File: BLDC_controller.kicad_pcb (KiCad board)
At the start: 4 copper layers, 50 x 35 mm, 95 parts, among them P2 CONN_01X06, P3 CONN_01X05, P5 CONN_01X05, Q1 PSMN2R0-30YLD, Q2 PSMN2R0-30YLD, Q3 PSMN2R0-30YLD, Q4 PSMN2R0-30YLD, Q5 PSMN2R0-30YLD, Q6 PSMN2R0-30YLD

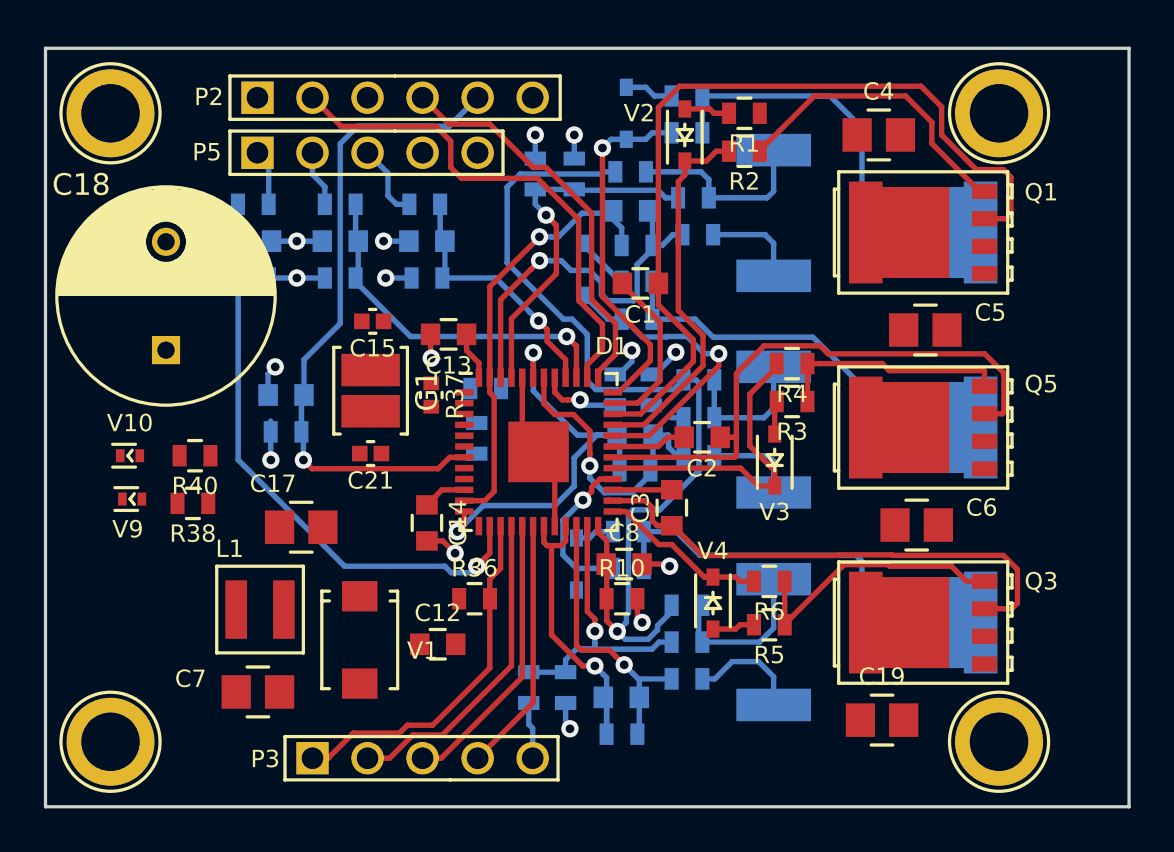
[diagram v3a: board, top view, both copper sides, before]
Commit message: keepouts added under sense resistors
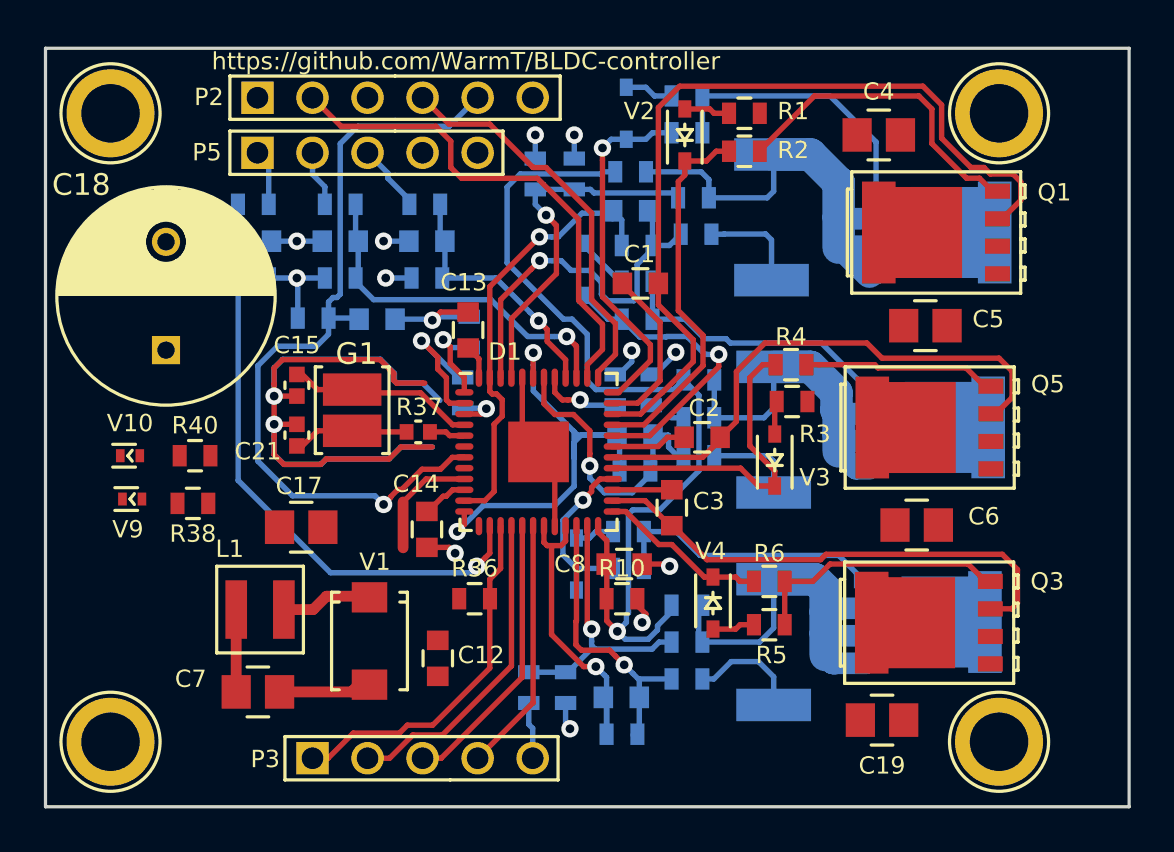
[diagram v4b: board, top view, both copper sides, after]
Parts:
- C15, C21: value C -> 10p
- moved C16 5.47 mm to (150.3, 91.5), turned to 0 degrees
- moved R39 5.40 mm to (147.3, 91.5)
- moved C15 4.58 mm to (146.6, 94.5), turned to 270 degrees
- moved C21 3.50 mm to (146.6, 96.8), turned to 90 degrees
- moved R29 2.71 mm to (154.6, 92.1), turned to 90 degrees
- moved R47 2.20 mm to (154.2, 94.9)
- moved R37 1.80 mm to (152.2, 96.7), turned to 180 degrees
- moved G1 1.24 mm to (149.2, 95.7)
- moved C13 0.92 mm to (154.5, 92.0), turned to 90 degrees
- moved C12 0.65 mm to (153.1, 107.2), turned to 270 degrees
- moved Q2 0.65 mm to (176.2, 87.5)
- moved Q1 0.60 mm to (176.1, 87.5)
- moved V1 0.45 mm to (149.9, 106.3)
- moved Q6 0.35 mm to (175.8, 96.5)
- moved Q5 0.30 mm to (175.8, 96.5)
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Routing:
- net GND: track 33.6 -> 81.5 mm, vias 8 -> 9
- net U_SENSE_P: track 8.90 -> 21.1 mm
- net W_SENSE_P: track 7.16 -> 19.3 mm
- net V_SENSE_P: track 6.58 -> 17.6 mm
- net /SW: track 0.00 -> 8.90 mm
- net /OSC_IN: track 0.00 -> 7.60 mm
- net /OP4N: track 0.00 -> 7.04 mm, vias 0 -> 1
- net /NRST: track 30.4 -> 37.3 mm
- net Net-(C21-Pad1): track 0.00 -> 6.60 mm
- net +3V3: track 13.2 -> 18.5 mm
- net /OP4P: track 0.00 -> 4.18 mm, vias 0 -> 1
- net Net-(D1-Pad3): track 0.00 -> 2.22 mm, vias 0 -> 1
- net /HSV: track 10.8 -> 8.63 mm
- net (no net): track 1.80 -> 0.00 mm, vias 1 -> 0
- net /V_ADC: track 20.7 -> 22.4 mm
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- added copper zone on B.Cu, net GND
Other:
- rule trace_min: 0.2 -> 0.15
- board text added: "https://github.com/WarmT/BLDC-controller"

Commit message: Layout ready for 1st review
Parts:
- removed C18: 680u, project_footprints:C_Radial_D10_L25_P5
- added REF**: VIA-0.8mm-0.4mm, project_footprints:VIA-0.8mm-0.4mm, F.Cu at (151.2, 97.8)
- added REF**: VIA-0.8mm-0.4mm, project_footprints:VIA-0.8mm-0.4mm, F.Cu at (149.9, 93.2)
- added REF**: VIA-1.2mm-0.8mm, project_footprints:VIA-1.2mm-0.8mm, F.Cu at (166.2, 113.2)
- added REF**: VIA-0.8mm-0.4mm, project_footprints:VIA-0.8mm-0.4mm, F.Cu at (147.8, 93.2)
- added REF**: VIA-0.8mm-0.4mm, project_footprints:VIA-0.8mm-0.4mm, F.Cu at (148.9, 93.2)
- added REF**: VIA-1.2mm-0.8mm, project_footprints:VIA-1.2mm-0.8mm, F.Cu at (172.8, 102.3)
- added REF**: VIA-1.2mm-0.8mm, project_footprints:VIA-1.2mm-0.8mm, F.Cu at (180.1, 100.7)
- added REF**: VIA-1.2mm-0.8mm, project_footprints:VIA-1.2mm-0.8mm, F.Cu at (174.9, 112.0)
- added REF**: VIA-1.2mm-0.8mm, project_footprints:VIA-1.2mm-0.8mm, F.Cu at (174.9, 109.9)
- added REF**: VIA-1.2mm-0.8mm, project_footprints:VIA-1.2mm-0.8mm, F.Cu at (174.4, 100.4)
- added REF**: VIA-1.2mm-0.8mm, project_footprints:VIA-1.2mm-0.8mm, F.Cu at (173.8, 91.3)
- added REF**: VIA-1.2mm-0.8mm, project_footprints:VIA-1.2mm-0.8mm, F.Cu at (179.5, 91.0)
- added REF**: VIA-1.2mm-0.8mm, project_footprints:VIA-1.2mm-0.8mm, F.Cu at (176.8, 84.0)
- added REF**: VIA-0.8mm-0.4mm, project_footprints:VIA-0.8mm-0.4mm, F.Cu at (149.8, 98.1)
- added REF**: VIA-1.2mm-0.8mm, project_footprints:VIA-1.2mm-0.8mm, F.Cu at (177.0, 79.0)
- added REF**: VIA-1.2mm-0.8mm, project_footprints:VIA-1.2mm-0.8mm, F.Cu at (177.0, 80.2)
- added REF**: VIA-1.2mm-0.8mm, project_footprints:VIA-1.2mm-0.8mm, F.Cu at (175.0, 80.2)
- added REF**: VIA-1.2mm-0.8mm, project_footprints:VIA-1.2mm-0.8mm, F.Cu at (175.0, 79.0)
- added REF**: VIA-1.2mm-0.8mm, project_footprints:VIA-1.2mm-0.8mm, F.Cu at (170.9, 81.8)
- added REF**: VIA-1.2mm-0.8mm, project_footprints:VIA-1.2mm-0.8mm, F.Cu at (169.7, 81.8)
- added REF**: VIA-1.2mm-0.8mm, project_footprints:VIA-1.2mm-0.8mm, F.Cu at (168.5, 81.8)
- added REF**: VIA-1.2mm-0.8mm, project_footprints:VIA-1.2mm-0.8mm, F.Cu at (167.3, 81.8)
- added REF**: VIA-1.2mm-0.8mm, project_footprints:VIA-1.2mm-0.8mm, F.Cu at (170.9, 80.7)
- added REF**: VIA-1.2mm-0.8mm, project_footprints:VIA-1.2mm-0.8mm, F.Cu at (169.7, 80.7)
- added REF**: VIA-0.8mm-0.4mm, project_footprints:VIA-0.8mm-0.4mm, F.Cu at (148.7, 98.1)
- added REF**: VIA-1.2mm-0.8mm, project_footprints:VIA-1.2mm-0.8mm, F.Cu at (168.5, 80.7)
- added REF**: VIA-1.2mm-0.8mm, project_footprints:VIA-1.2mm-0.8mm, F.Cu at (167.3, 80.7)
- added REF**: VIA-1.2mm-0.8mm, project_footprints:VIA-1.2mm-0.8mm, F.Cu at (170.9, 79.5)
- added REF**: VIA-1.2mm-0.8mm, project_footprints:VIA-1.2mm-0.8mm, F.Cu at (169.7, 79.5)
- added REF**: VIA-1.2mm-0.8mm, project_footprints:VIA-1.2mm-0.8mm, F.Cu at (168.5, 79.5)
- added REF**: VIA-1.2mm-0.8mm, project_footprints:VIA-1.2mm-0.8mm, F.Cu at (169.7, 103.6)
- added REF**: VIA-1.2mm-0.8mm, project_footprints:VIA-1.2mm-0.8mm, F.Cu at (168.5, 103.6)
- added REF**: VIA-1.2mm-0.8mm, project_footprints:VIA-1.2mm-0.8mm, F.Cu at (167.3, 103.6)
- added REF**: VIA-1.2mm-0.8mm, project_footprints:VIA-1.2mm-0.8mm, F.Cu at (170.9, 103.6)
- added REF**: VIA-1.2mm-0.8mm, project_footprints:VIA-1.2mm-0.8mm, F.Cu at (169.7, 102.4)
- added REF**: VIA-0.8mm-0.4mm, project_footprints:VIA-0.8mm-0.4mm, F.Cu at (146.6, 93.1)
- added REF**: VIA-1.2mm-0.8mm, project_footprints:VIA-1.2mm-0.8mm, F.Cu at (168.5, 102.4)
- added REF**: VIA-1.2mm-0.8mm, project_footprints:VIA-1.2mm-0.8mm, F.Cu at (167.3, 102.4)
- added REF**: VIA-1.2mm-0.8mm, project_footprints:VIA-1.2mm-0.8mm, F.Cu at (170.9, 102.4)
- added REF**: VIA-1.2mm-0.8mm, project_footprints:VIA-1.2mm-0.8mm, F.Cu at (169.7, 101.2)
- added REF**: VIA-1.2mm-0.8mm, project_footprints:VIA-1.2mm-0.8mm, F.Cu at (168.5, 101.2)
- added REF**: VIA-1.2mm-0.8mm, project_footprints:VIA-1.2mm-0.8mm, F.Cu at (167.3, 101.2)
- added REF**: VIA-1.2mm-0.8mm, project_footprints:VIA-1.2mm-0.8mm, F.Cu at (170.9, 101.2)
- added REF**: VIA-1.2mm-0.8mm, project_footprints:VIA-1.2mm-0.8mm, F.Cu at (184.2, 108.4)
- added REF**: VIA-1.2mm-0.8mm, project_footprints:VIA-1.2mm-0.8mm, F.Cu at (182.9, 108.4)
- added REF**: VIA-1.2mm-0.8mm, project_footprints:VIA-1.2mm-0.8mm, F.Cu at (181.8, 108.4)
- added REF**: VIA-0.8mm-0.4mm, project_footprints:VIA-0.8mm-0.4mm, F.Cu at (147.5, 98.2)
- added REF**: VIA-1.2mm-0.8mm, project_footprints:VIA-1.2mm-0.8mm, F.Cu at (184.2, 107.2)
- added REF**: VIA-1.2mm-0.8mm, project_footprints:VIA-1.2mm-0.8mm, F.Cu at (182.9, 107.2)
- added REF**: VIA-1.2mm-0.8mm, project_footprints:VIA-1.2mm-0.8mm, F.Cu at (181.8, 107.2)
- added REF**: VIA-1.2mm-0.8mm, project_footprints:VIA-1.2mm-0.8mm, F.Cu at (184.2, 106.0)
- added REF**: VIA-1.2mm-0.8mm, project_footprints:VIA-1.2mm-0.8mm, F.Cu at (182.9, 106.0)
- added REF**: VIA-1.2mm-0.8mm, project_footprints:VIA-1.2mm-0.8mm, F.Cu at (181.8, 106.0)
- added REF**: VIA-1.2mm-0.8mm, project_footprints:VIA-1.2mm-0.8mm, F.Cu at (184.2, 104.8)
- added REF**: VIA-1.2mm-0.8mm, project_footprints:VIA-1.2mm-0.8mm, F.Cu at (182.9, 104.8)
- added REF**: VIA-1.2mm-0.8mm, project_footprints:VIA-1.2mm-0.8mm, F.Cu at (181.8, 104.8)
- added REF**: VIA-1.2mm-0.8mm, project_footprints:VIA-1.2mm-0.8mm, F.Cu at (184.2, 99.6)
- added REF**: VIA-0.8mm-0.4mm, project_footprints:VIA-0.8mm-0.4mm, F.Cu at (145.5, 97.4)
- added REF**: VIA-1.2mm-0.8mm, project_footprints:VIA-1.2mm-0.8mm, F.Cu at (182.9, 99.6)
- added REF**: VIA-1.2mm-0.8mm, project_footprints:VIA-1.2mm-0.8mm, F.Cu at (181.8, 99.6)
- added REF**: VIA-1.2mm-0.8mm, project_footprints:VIA-1.2mm-0.8mm, F.Cu at (184.2, 98.4)
- added REF**: VIA-1.2mm-0.8mm, project_footprints:VIA-1.2mm-0.8mm, F.Cu at (182.9, 98.4)
- added REF**: VIA-1.2mm-0.8mm, project_footprints:VIA-1.2mm-0.8mm, F.Cu at (181.8, 98.4)
- added REF**: VIA-1.2mm-0.8mm, project_footprints:VIA-1.2mm-0.8mm, F.Cu at (184.2, 97.2)
- added REF**: VIA-1.2mm-0.8mm, project_footprints:VIA-1.2mm-0.8mm, F.Cu at (182.9, 97.2)
- added REF**: VIA-1.2mm-0.8mm, project_footprints:VIA-1.2mm-0.8mm, F.Cu at (181.8, 97.2)
- added REF**: VIA-1.2mm-0.8mm, project_footprints:VIA-1.2mm-0.8mm, F.Cu at (184.2, 96.0)
- added REF**: VIA-1.2mm-0.8mm, project_footprints:VIA-1.2mm-0.8mm, F.Cu at (182.9, 96.0)
- added REF**: VIA-0.8mm-0.4mm, project_footprints:VIA-0.8mm-0.4mm, F.Cu at (145.6, 93.9)
- added REF**: VIA-1.2mm-0.8mm, project_footprints:VIA-1.2mm-0.8mm, F.Cu at (181.8, 96.0)
- added REF**: VIA-1.2mm-0.8mm, project_footprints:VIA-1.2mm-0.8mm, F.Cu at (184.2, 90.7)
- added REF**: VIA-1.2mm-0.8mm, project_footprints:VIA-1.2mm-0.8mm, F.Cu at (182.9, 90.7)
- added REF**: VIA-1.2mm-0.8mm, project_footprints:VIA-1.2mm-0.8mm, F.Cu at (181.8, 90.7)
- added REF**: VIA-1.2mm-0.8mm, project_footprints:VIA-1.2mm-0.8mm, F.Cu at (184.2, 89.5)
- added REF**: VIA-1.2mm-0.8mm, project_footprints:VIA-1.2mm-0.8mm, F.Cu at (182.9, 89.5)
- added REF**: VIA-1.2mm-0.8mm, project_footprints:VIA-1.2mm-0.8mm, F.Cu at (181.8, 89.5)
- added REF**: VIA-1.2mm-0.8mm, project_footprints:VIA-1.2mm-0.8mm, F.Cu at (184.2, 88.3)
- added REF**: VIA-1.2mm-0.8mm, project_footprints:VIA-1.2mm-0.8mm, F.Cu at (182.9, 88.3)
- added REF**: VIA-1.2mm-0.8mm, project_footprints:VIA-1.2mm-0.8mm, F.Cu at (181.8, 88.3)
- added REF**: VIA-0.8mm-0.4mm, project_footprints:VIA-0.8mm-0.4mm, F.Cu at (152.2, 94.1)
- added REF**: VIA-1.2mm-0.8mm, project_footprints:VIA-1.2mm-0.8mm, F.Cu at (184.2, 87.1)
- added REF**: VIA-1.2mm-0.8mm, project_footprints:VIA-1.2mm-0.8mm, F.Cu at (182.9, 87.1)
- added REF**: VIA-1.2mm-0.8mm, project_footprints:VIA-1.2mm-0.8mm, F.Cu at (181.8, 87.1)
- added REF**: VIA-1.2mm-0.8mm, project_footprints:VIA-1.2mm-0.8mm, F.Cu at (157.0, 95.5)
- added REF**: VIA-1.2mm-0.8mm, project_footprints:VIA-1.2mm-0.8mm, F.Cu at (172.2, 114.5)
- added REF**: VIA-1.2mm-0.8mm, project_footprints:VIA-1.2mm-0.8mm, F.Cu at (171.1, 114.5)
- added REF**: VIA-1.2mm-0.8mm, project_footprints:VIA-1.2mm-0.8mm, F.Cu at (169.8, 114.5)
- added REF**: VIA-1.2mm-0.8mm, project_footprints:VIA-1.2mm-0.8mm, F.Cu at (168.7, 114.5)
- added REF**: VIA-1.2mm-0.8mm, project_footprints:VIA-1.2mm-0.8mm, F.Cu at (167.4, 114.5)
- added REF**: VIA-0.8mm-0.4mm, project_footprints:VIA-0.8mm-0.4mm, F.Cu at (151.0, 93.4)
- added REF**: VIA-1.2mm-0.8mm, project_footprints:VIA-1.2mm-0.8mm, F.Cu at (166.2, 114.5)
- added REF**: VIA-1.2mm-0.8mm, project_footprints:VIA-1.2mm-0.8mm, F.Cu at (172.2, 113.2)
- added REF**: VIA-1.2mm-0.8mm, project_footprints:VIA-1.2mm-0.8mm, F.Cu at (171.1, 113.2)
- added REF**: VIA-1.2mm-0.8mm, project_footprints:VIA-1.2mm-0.8mm, F.Cu at (169.8, 113.2)
- added REF**: VIA-1.2mm-0.8mm, project_footprints:VIA-1.2mm-0.8mm, F.Cu at (168.7, 113.2)
- added REF**: VIA-1.2mm-0.8mm, project_footprints:VIA-1.2mm-0.8mm, F.Cu at (167.4, 113.2)
- added REF**: VIA-1.2mm-0.8mm, project_footprints:VIA-1.2mm-0.8mm, F.Cu at (167.3, 79.5)
- moved V10 26.3 mm to (161.0, 112.1)
- moved R40 25.9 mm to (163.6, 112.1)
- moved V9 22.3 mm to (159.3, 109.0)
- moved R38 22.0 mm to (161.8, 109.1)
- moved C12 8.53 mm to (148.6, 99.9), turned to 180 degrees
- moved C1 4.24 mm to (161.6, 85.7)
- moved C19 3.52 mm to (177.0, 110.9), turned to 270 degrees
- moved REF** 3.48 mm to (182.0, 112.8)
- moved REF** 3.09 mm to (182.0, 81.3)
- moved C4 2.78 mm to (176.0, 81.9)
- moved R2 2.77 mm to (164.5, 83.4)
- moved R1 2.77 mm to (164.5, 81.7)
- moved C17 2.69 mm to (149.3, 102.1), turned to 180 degrees
- moved R7 2.48 mm to (170.2, 108.3)
- moved V2 2.38 mm to (162.2, 82.4)
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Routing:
- net GND: track 81.5 -> 114.7 mm, vias 9 -> 20
- net +12V: track 0.00 -> 25.7 mm, vias 0 -> 3
- net /OUTW: track 23.5 -> 37.0 mm, vias 0 -> 1
- net +3V3: track 18.5 -> 30.0 mm, vias 6 -> 9
- net /OUTU: track 39.3 -> 49.9 mm, vias 0 -> 1
- net V_SENSE_P: track 17.6 -> 7.63 mm, vias 0 -> 2
- net /HSU: track 14.8 -> 24.0 mm, vias 0 -> 2
- net U_SENSE_P: track 21.1 -> 12.4 mm, vias 0 -> 2
- net /HSV: track 8.63 -> 17.2 mm, vias 0 -> 2
- net /OUTV: track 25.1 -> 33.3 mm, vias 0 -> 1
- net /LSV: track 13.1 -> 20.6 mm, vias 0 -> 2
- net W_SENSE_P: track 19.3 -> 12.2 mm, vias 0 -> 2
- net /LSU: track 12.9 -> 19.8 mm, vias 0 -> 2
- net /LSW: track 13.5 -> 20.0 mm, vias 0 -> 2
- net /HSW: track 12.2 -> 18.6 mm, vias 0 -> 2
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- added copper zone on F.Cu, net +12V
- added copper zone on In1.Cu, net +12V
- added copper zone on In2.Cu, net +12V
- added copper zone on In1.Cu, net +3V3
- added copper zone on B.Cu, net /OUTU
- added copper zone on F.Cu, net /OUTU
- added copper zone on In2.Cu, net /OUTU
- added copper zone on B.Cu, net /OUTV
- added copper zone on F.Cu, net /OUTV
- added copper zone on In2.Cu, net /OUTV
- added copper zone on B.Cu, net /OUTW
- added copper zone on F.Cu, net /OUTW
- added copper zone on In2.Cu, net /OUTW
- added copper zone on F.Cu, net GND
- added copper zone on In2.Cu, net GND
- added copper zone on B.Cu, net U_SENSE_P
- added copper zone on B.Cu, net V_SENSE_P
- added copper zone on B.Cu, net W_SENSE_P
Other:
- board size 50 x 35 mm -> 50 x 38 mm
- rule trace_min: 0.15 -> 0.25
- board text added: "1"
- board text added: "2"
- board text added: "3"
- board text added: "4"
- board text added: "github.com/WarmT/BLDC-controller 1.0"
- board text removed: "https://github.com/WarmT/BLDC-controller"

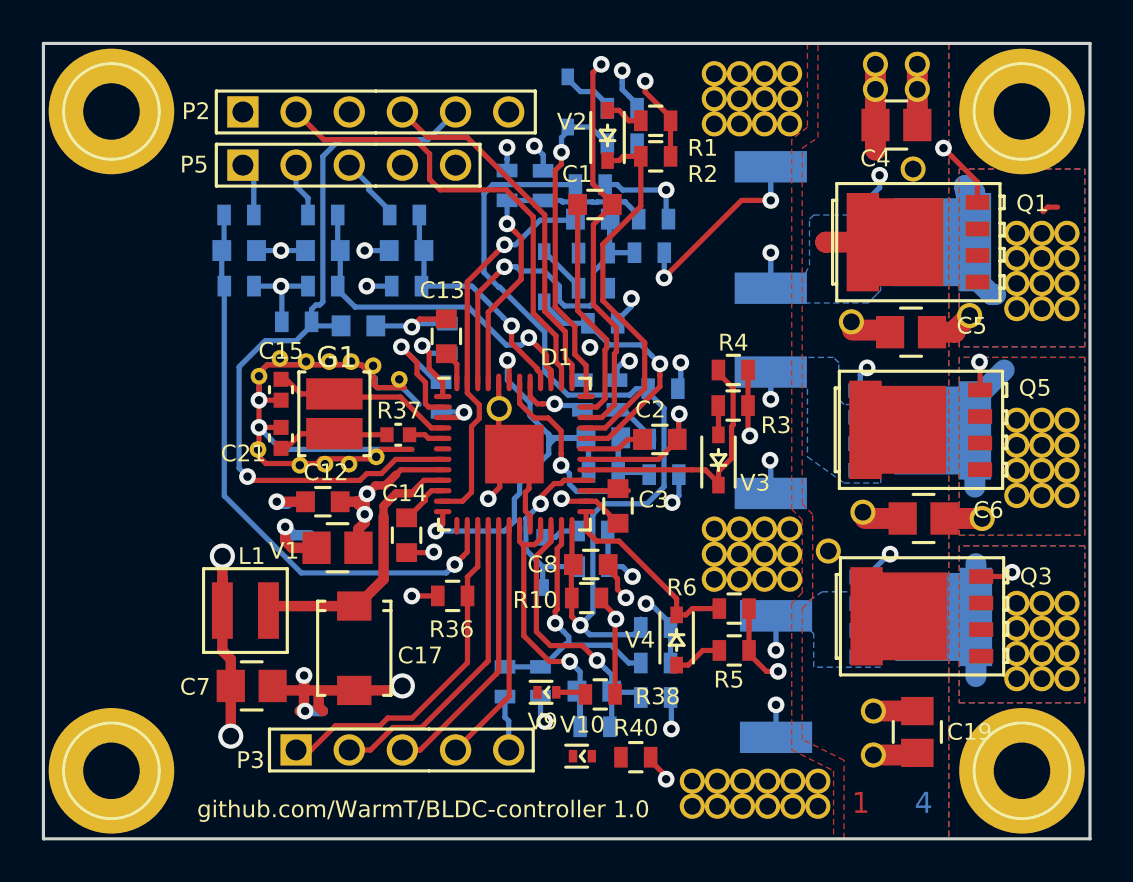
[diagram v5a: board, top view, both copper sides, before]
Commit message: change thermal vias smaller
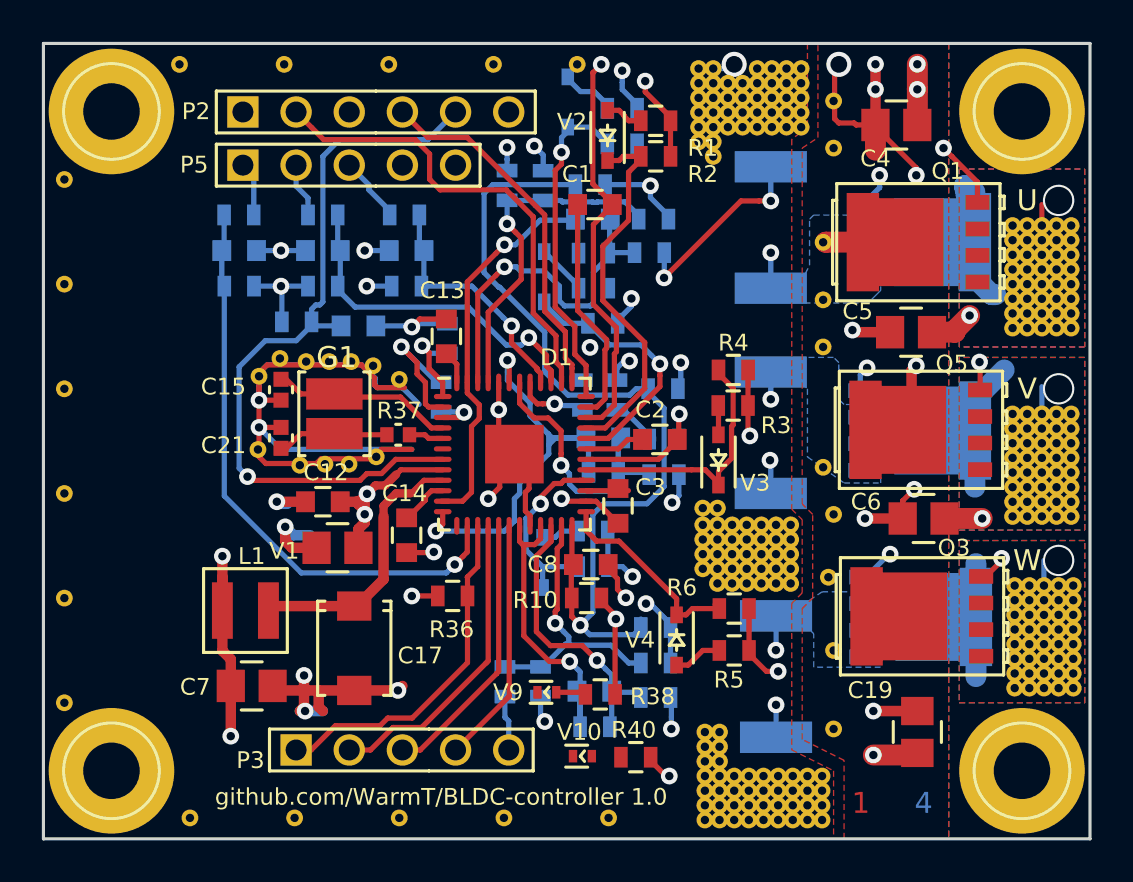
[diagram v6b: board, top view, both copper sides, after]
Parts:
- removed the REF** at (166.2, 113.2)
- removed the REF** at (172.8, 102.3)
- removed the REF** at (180.1, 100.7)
- removed the REF** at (174.9, 112.0)
- removed the REF** at (174.9, 109.9)
- removed the REF** at (174.4, 100.4)
- removed the REF** at (173.8, 91.3)
- removed the REF** at (179.5, 91.0)
- removed the REF** at (176.8, 84.0)
- removed the REF** at (177.0, 79.0)
- removed the REF** at (177.0, 80.2)
- removed the REF** at (175.0, 80.2)
- removed the REF** at (175.0, 79.0)
- removed the REF** at (170.9, 81.8)
- removed the REF** at (169.7, 81.8)
- removed the REF** at (168.5, 81.8)
- removed the REF** at (167.3, 81.8)
- removed the REF** at (170.9, 80.7)
- removed the REF** at (169.7, 80.7)
- removed the REF** at (168.5, 80.7)
- removed the REF** at (167.3, 80.7)
- removed the REF** at (170.9, 79.5)
- removed the REF** at (169.7, 79.5)
- removed the REF** at (168.5, 79.5)
- removed the REF** at (169.7, 103.6)
- removed the REF** at (168.5, 103.6)
- removed the REF** at (167.3, 103.6)
- removed the REF** at (170.9, 103.6)
- removed the REF** at (169.7, 102.4)
- removed the REF** at (168.5, 102.4)
- removed the REF** at (167.3, 102.4)
- removed the REF** at (170.9, 102.4)
- removed the REF** at (169.7, 101.2)
- removed the REF** at (168.5, 101.2)
- removed the REF** at (167.3, 101.2)
- removed the REF** at (170.9, 101.2)
- removed the REF** at (184.2, 108.4)
- removed the REF** at (182.9, 108.4)
- removed the REF** at (181.8, 108.4)
- removed the REF** at (184.2, 107.2)
- removed the REF** at (182.9, 107.2)
- removed the REF** at (181.8, 107.2)
- removed the REF** at (184.2, 106.0)
- removed the REF** at (182.9, 106.0)
- removed the REF** at (181.8, 106.0)
- removed the REF** at (184.2, 104.8)
- removed the REF** at (182.9, 104.8)
- removed the REF** at (181.8, 104.8)
- removed the REF** at (184.2, 99.6)
- removed the REF** at (182.9, 99.6)
- removed the REF** at (181.8, 99.6)
- removed the REF** at (184.2, 98.4)
- removed the REF** at (182.9, 98.4)
- removed the REF** at (181.8, 98.4)
- removed the REF** at (184.2, 97.2)
- removed the REF** at (182.9, 97.2)
- removed the REF** at (181.8, 97.2)
- removed the REF** at (184.2, 96.0)
- removed the REF** at (182.9, 96.0)
- removed the REF** at (181.8, 96.0)
- removed the REF** at (184.2, 90.7)
- removed the REF** at (182.9, 90.7)
- removed the REF** at (181.8, 90.7)
- removed the REF** at (184.2, 89.5)
- removed the REF** at (182.9, 89.5)
- removed the REF** at (181.8, 89.5)
- removed the REF** at (184.2, 88.3)
- removed the REF** at (182.9, 88.3)
- removed the REF** at (181.8, 88.3)
- removed the REF** at (184.2, 87.1)
- removed the REF** at (182.9, 87.1)
- removed the REF** at (181.8, 87.1)
- removed the REF** at (157.0, 95.5)
- removed the REF** at (172.2, 114.5)
- removed the REF** at (171.1, 114.5)
- removed the REF** at (169.8, 114.5)
- removed the REF** at (168.7, 114.5)
- removed the REF** at (167.4, 114.5)
- removed the REF** at (166.2, 114.5)
- removed the REF** at (172.2, 113.2)
- removed the REF** at (171.1, 113.2)
- removed the REF** at (169.8, 113.2)
- removed the REF** at (168.7, 113.2)
- removed the REF** at (167.4, 113.2)
- removed the REF** at (167.3, 79.5)
- added REF**: VIA-0.8mm-0.4mm, project_footprints:VIA-0.8mm-0.4mm, F.Cu at (162.2, 115.0)
- added REF**: VIA-0.8mm-0.4mm, project_footprints:VIA-0.8mm-0.4mm, F.Cu at (136.2, 94.5)
- added REF**: VIA-0.8mm-0.4mm, project_footprints:VIA-0.8mm-0.4mm, F.Cu at (181.6, 96.4)
- added REF**: VIA-0.8mm-0.4mm, project_footprints:VIA-0.8mm-0.4mm, F.Cu at (184.3, 95.7)
- added REF**: VIA-0.8mm-0.4mm, project_footprints:VIA-0.8mm-0.4mm, F.Cu at (183.7, 95.7)
- added REF**: VIA-0.8mm-0.4mm, project_footprints:VIA-0.8mm-0.4mm, F.Cu at (182.9, 95.7)
- added REF**: VIA-0.8mm-0.4mm, project_footprints:VIA-0.8mm-0.4mm, F.Cu at (182.2, 95.7)
- added REF**: VIA-0.8mm-0.4mm, project_footprints:VIA-0.8mm-0.4mm, F.Cu at (181.7, 103.9)
- added REF**: VIA-0.8mm-0.4mm, project_footprints:VIA-0.8mm-0.4mm, F.Cu at (184.3, 91.6)
- added REF**: VIA-0.8mm-0.4mm, project_footprints:VIA-0.8mm-0.4mm, F.Cu at (183.7, 91.6)
- added REF**: VIA-0.8mm-0.4mm, project_footprints:VIA-0.8mm-0.4mm, F.Cu at (182.9, 91.6)
- added REF**: VIA-0.8mm-0.4mm, project_footprints:VIA-0.8mm-0.4mm, F.Cu at (182.2, 91.6)
- added REF**: VIA-0.8mm-0.4mm, project_footprints:VIA-0.8mm-0.4mm, F.Cu at (136.2, 99.5)
- added REF**: VIA-0.8mm-0.4mm, project_footprints:VIA-0.8mm-0.4mm, F.Cu at (181.6, 91.6)
- added REF**: VIA-0.8mm-0.4mm, project_footprints:VIA-0.8mm-0.4mm, F.Cu at (184.3, 90.9)
- added REF**: VIA-0.8mm-0.4mm, project_footprints:VIA-0.8mm-0.4mm, F.Cu at (183.7, 90.9)
- added REF**: VIA-0.8mm-0.4mm, project_footprints:VIA-0.8mm-0.4mm, F.Cu at (182.9, 90.9)
- added REF**: VIA-0.8mm-0.4mm, project_footprints:VIA-0.8mm-0.4mm, F.Cu at (182.2, 90.9)
- added REF**: VIA-0.8mm-0.4mm, project_footprints:VIA-0.8mm-0.4mm, F.Cu at (181.6, 90.9)
- added REF**: VIA-0.8mm-0.4mm, project_footprints:VIA-0.8mm-0.4mm, F.Cu at (184.3, 90.2)
- added REF**: VIA-0.8mm-0.4mm, project_footprints:VIA-0.8mm-0.4mm, F.Cu at (183.7, 90.2)
- added REF**: VIA-0.8mm-0.4mm, project_footprints:VIA-0.8mm-0.4mm, F.Cu at (182.9, 90.2)
- added REF**: VIA-0.8mm-0.4mm, project_footprints:VIA-0.8mm-0.4mm, F.Cu at (182.2, 90.2)
- added REF**: VIA-0.8mm-0.4mm, project_footprints:VIA-0.8mm-0.4mm, F.Cu at (136.2, 104.5)
- added REF**: VIA-0.8mm-0.4mm, project_footprints:VIA-0.8mm-0.4mm, F.Cu at (181.6, 90.2)
- added REF**: VIA-0.8mm-0.4mm, project_footprints:VIA-0.8mm-0.4mm, F.Cu at (184.3, 89.5)
- added REF**: VIA-0.8mm-0.4mm, project_footprints:VIA-0.8mm-0.4mm, F.Cu at (183.7, 89.5)
- added REF**: VIA-0.8mm-0.4mm, project_footprints:VIA-0.8mm-0.4mm, F.Cu at (182.9, 89.5)
- added REF**: VIA-0.8mm-0.4mm, project_footprints:VIA-0.8mm-0.4mm, F.Cu at (182.2, 89.5)
- added REF**: VIA-0.8mm-0.4mm, project_footprints:VIA-0.8mm-0.4mm, F.Cu at (181.6, 89.5)
- added REF**: VIA-0.8mm-0.4mm, project_footprints:VIA-0.8mm-0.4mm, F.Cu at (184.3, 88.8)
- added REF**: VIA-0.8mm-0.4mm, project_footprints:VIA-0.8mm-0.4mm, F.Cu at (183.7, 88.8)
- added REF**: VIA-0.8mm-0.4mm, project_footprints:VIA-0.8mm-0.4mm, F.Cu at (182.9, 88.8)
- added REF**: VIA-0.8mm-0.4mm, project_footprints:VIA-0.8mm-0.4mm, F.Cu at (182.2, 88.8)
- added REF**: VIA-0.8mm-0.4mm, project_footprints:VIA-0.8mm-0.4mm, F.Cu at (142.2, 115.0)
- added REF**: VIA-0.8mm-0.4mm, project_footprints:VIA-0.8mm-0.4mm, F.Cu at (181.6, 88.8)
- added REF**: VIA-0.8mm-0.4mm, project_footprints:VIA-0.8mm-0.4mm, F.Cu at (184.3, 88.1)
- added REF**: VIA-0.8mm-0.4mm, project_footprints:VIA-0.8mm-0.4mm, F.Cu at (183.7, 88.1)
- added REF**: VIA-0.8mm-0.4mm, project_footprints:VIA-0.8mm-0.4mm, F.Cu at (182.9, 88.1)
- added REF**: VIA-0.8mm-0.4mm, project_footprints:VIA-0.8mm-0.4mm, F.Cu at (182.2, 88.1)
- added REF**: VIA-0.8mm-0.4mm, project_footprints:VIA-0.8mm-0.4mm, F.Cu at (181.6, 88.1)
- added REF**: VIA-0.8mm-0.4mm, project_footprints:VIA-0.8mm-0.4mm, F.Cu at (184.3, 87.4)
- added REF**: VIA-0.8mm-0.4mm, project_footprints:VIA-0.8mm-0.4mm, F.Cu at (183.7, 87.4)
- added REF**: VIA-0.8mm-0.4mm, project_footprints:VIA-0.8mm-0.4mm, F.Cu at (182.9, 87.4)
- added REF**: VIA-0.8mm-0.4mm, project_footprints:VIA-0.8mm-0.4mm, F.Cu at (182.2, 87.4)
- added REF**: VIA-0.8mm-0.4mm, project_footprints:VIA-0.8mm-0.4mm, F.Cu at (147.2, 115.0)
- added REF**: VIA-0.8mm-0.4mm, project_footprints:VIA-0.8mm-0.4mm, F.Cu at (181.6, 87.4)
- added REF**: VIA-0.8mm-0.4mm, project_footprints:VIA-0.8mm-0.4mm, F.Cu at (181.6, 95.7)
- added REF**: VIA-0.8mm-0.4mm, project_footprints:VIA-0.8mm-0.4mm, F.Cu at (184.3, 86.7)
- added REF**: VIA-0.8mm-0.4mm, project_footprints:VIA-0.8mm-0.4mm, F.Cu at (183.7, 86.7)
- added REF**: VIA-0.8mm-0.4mm, project_footprints:VIA-0.8mm-0.4mm, F.Cu at (182.9, 86.7)
- added REF**: VIA-0.8mm-0.4mm, project_footprints:VIA-0.8mm-0.4mm, F.Cu at (182.2, 86.7)
- added REF**: VIA-0.8mm-0.4mm, project_footprints:VIA-0.8mm-0.4mm, F.Cu at (181.6, 86.7)
- added REF**: VIA-0.8mm-0.4mm, project_footprints:VIA-0.8mm-0.4mm, F.Cu at (167.2, 83.4)
- added REF**: VIA-0.8mm-0.4mm, project_footprints:VIA-0.8mm-0.4mm, F.Cu at (167.4, 100.2)
- added REF**: VIA-0.8mm-0.4mm, project_footprints:VIA-0.8mm-0.4mm, F.Cu at (166.8, 100.2)
- added REF**: VIA-0.8mm-0.4mm, project_footprints:VIA-0.8mm-0.4mm, F.Cu at (152.2, 115.0)
- added REF**: VIA-0.8mm-0.4mm, project_footprints:VIA-0.8mm-0.4mm, F.Cu at (171.4, 82.0)
- added REF**: VIA-0.8mm-0.4mm, project_footprints:VIA-0.8mm-0.4mm, F.Cu at (170.8, 82.0)
- added REF**: VIA-0.8mm-0.4mm, project_footprints:VIA-0.8mm-0.4mm, F.Cu at (170.1, 82.0)
- added REF**: VIA-0.8mm-0.4mm, project_footprints:VIA-0.8mm-0.4mm, F.Cu at (169.3, 82.0)
- added REF**: VIA-0.8mm-0.4mm, project_footprints:VIA-0.8mm-0.4mm, F.Cu at (168.7, 82.0)
- added REF**: VIA-0.8mm-0.4mm, project_footprints:VIA-0.8mm-0.4mm, F.Cu at (167.9, 82.0)
- added REF**: VIA-0.8mm-0.4mm, project_footprints:VIA-0.8mm-0.4mm, F.Cu at (167.2, 82.0)
- added REF**: VIA-0.8mm-0.4mm, project_footprints:VIA-0.8mm-0.4mm, F.Cu at (166.6, 82.0)
- added REF**: VIA-0.8mm-0.4mm, project_footprints:VIA-0.8mm-0.4mm, F.Cu at (171.4, 81.3)
- added REF**: VIA-0.8mm-0.4mm, project_footprints:VIA-0.8mm-0.4mm, F.Cu at (170.8, 81.3)
- added REF**: VIA-0.8mm-0.4mm, project_footprints:VIA-0.8mm-0.4mm, F.Cu at (157.2, 115.0)
- added REF**: VIA-0.8mm-0.4mm, project_footprints:VIA-0.8mm-0.4mm, F.Cu at (170.1, 81.3)
- added REF**: VIA-0.8mm-0.4mm, project_footprints:VIA-0.8mm-0.4mm, F.Cu at (169.3, 81.3)
- added REF**: VIA-0.8mm-0.4mm, project_footprints:VIA-0.8mm-0.4mm, F.Cu at (168.7, 81.3)
- added REF**: VIA-0.8mm-0.4mm, project_footprints:VIA-0.8mm-0.4mm, F.Cu at (167.9, 81.3)
- added REF**: VIA-0.8mm-0.4mm, project_footprints:VIA-0.8mm-0.4mm, F.Cu at (167.2, 81.3)
- added REF**: VIA-0.8mm-0.4mm, project_footprints:VIA-0.8mm-0.4mm, F.Cu at (166.6, 81.3)
- added REF**: VIA-0.8mm-0.4mm, project_footprints:VIA-0.8mm-0.4mm, F.Cu at (171.4, 80.6)
- added REF**: VIA-0.8mm-0.4mm, project_footprints:VIA-0.8mm-0.4mm, F.Cu at (170.8, 80.6)
- added REF**: VIA-0.8mm-0.4mm, project_footprints:VIA-0.8mm-0.4mm, F.Cu at (170.1, 80.6)
- added REF**: VIA-0.8mm-0.4mm, project_footprints:VIA-0.8mm-0.4mm, F.Cu at (169.3, 80.6)
- added REF**: VIA-0.8mm-0.4mm, project_footprints:VIA-0.8mm-0.4mm, F.Cu at (173.0, 80.8)
- added REF**: VIA-0.8mm-0.4mm, project_footprints:VIA-0.8mm-0.4mm, F.Cu at (168.7, 80.6)
- added REF**: VIA-0.8mm-0.4mm, project_footprints:VIA-0.8mm-0.4mm, F.Cu at (167.9, 80.6)
- added REF**: VIA-0.8mm-0.4mm, project_footprints:VIA-0.8mm-0.4mm, F.Cu at (167.2, 80.6)
- added REF**: VIA-0.8mm-0.4mm, project_footprints:VIA-0.8mm-0.4mm, F.Cu at (166.6, 80.6)
- added REF**: VIA-0.8mm-0.4mm, project_footprints:VIA-0.8mm-0.4mm, F.Cu at (171.4, 79.9)
- added REF**: VIA-0.8mm-0.4mm, project_footprints:VIA-0.8mm-0.4mm, F.Cu at (170.8, 79.9)
- added REF**: VIA-0.8mm-0.4mm, project_footprints:VIA-0.8mm-0.4mm, F.Cu at (170.1, 79.9)
- added REF**: VIA-0.8mm-0.4mm, project_footprints:VIA-0.8mm-0.4mm, F.Cu at (169.3, 79.9)
- added REF**: VIA-0.8mm-0.4mm, project_footprints:VIA-0.8mm-0.4mm, F.Cu at (168.7, 79.9)
- added REF**: VIA-0.8mm-0.4mm, project_footprints:VIA-0.8mm-0.4mm, F.Cu at (167.9, 79.9)
- added REF**: VIA-0.8mm-0.4mm, project_footprints:VIA-0.8mm-0.4mm, F.Cu at (173.0, 83.0)
- added REF**: VIA-0.8mm-0.4mm, project_footprints:VIA-0.8mm-0.4mm, F.Cu at (167.2, 79.9)
- added REF**: VIA-0.8mm-0.4mm, project_footprints:VIA-0.8mm-0.4mm, F.Cu at (166.6, 79.9)
- added REF**: VIA-0.8mm-0.4mm, project_footprints:VIA-0.8mm-0.4mm, F.Cu at (167.2, 82.7)
- added REF**: VIA-0.8mm-0.4mm, project_footprints:VIA-0.8mm-0.4mm, F.Cu at (166.6, 82.7)
- added REF**: VIA-0.8mm-0.4mm, project_footprints:VIA-0.8mm-0.4mm, F.Cu at (171.4, 79.2)
- added REF**: VIA-0.8mm-0.4mm, project_footprints:VIA-0.8mm-0.4mm, F.Cu at (170.8, 79.2)
- added REF**: VIA-0.8mm-0.4mm, project_footprints:VIA-0.8mm-0.4mm, F.Cu at (170.1, 79.2)
- added REF**: VIA-0.8mm-0.4mm, project_footprints:VIA-0.8mm-0.4mm, F.Cu at (169.3, 79.2)
- added REF**: VIA-0.8mm-0.4mm, project_footprints:VIA-0.8mm-0.4mm, F.Cu at (167.2, 79.2)
- added REF**: VIA-0.8mm-0.4mm, project_footprints:VIA-0.8mm-0.4mm, F.Cu at (166.6, 79.2)
- added REF**: VIA-0.8mm-0.4mm, project_footprints:VIA-0.8mm-0.4mm, F.Cu at (172.5, 87.5)
- added REF**: VIA-0.8mm-0.4mm, project_footprints:VIA-0.8mm-0.4mm, F.Cu at (167.6, 112.3)
- added REF**: VIA-0.8mm-0.4mm, project_footprints:VIA-0.8mm-0.4mm, F.Cu at (166.8, 112.3)
- added REF**: VIA-0.8mm-0.4mm, project_footprints:VIA-0.8mm-0.4mm, F.Cu at (167.6, 111.6)
- added REF**: VIA-0.8mm-0.4mm, project_footprints:VIA-0.8mm-0.4mm, F.Cu at (166.8, 111.6)
- added REF**: VIA-0.8mm-0.4mm, project_footprints:VIA-0.8mm-0.4mm, F.Cu at (167.6, 110.9)
- added REF**: VIA-0.8mm-0.4mm, project_footprints:VIA-0.8mm-0.4mm, F.Cu at (166.8, 110.9)
- added REF**: VIA-0.8mm-0.4mm, project_footprints:VIA-0.8mm-0.4mm, F.Cu at (170.9, 103.8)
- added REF**: VIA-0.8mm-0.4mm, project_footprints:VIA-0.8mm-0.4mm, F.Cu at (170.2, 103.8)
- added REF**: VIA-0.8mm-0.4mm, project_footprints:VIA-0.8mm-0.4mm, F.Cu at (169.6, 103.8)
- added REF**: VIA-0.8mm-0.4mm, project_footprints:VIA-0.8mm-0.4mm, F.Cu at (168.8, 103.8)
- added REF**: VIA-0.8mm-0.4mm, project_footprints:VIA-0.8mm-0.4mm, F.Cu at (160.8, 79.0)
- added REF**: VIA-0.8mm-0.4mm, project_footprints:VIA-0.8mm-0.4mm, F.Cu at (172.5, 90.3)
- added REF**: VIA-0.8mm-0.4mm, project_footprints:VIA-0.8mm-0.4mm, F.Cu at (168.2, 103.8)
- added REF**: VIA-0.8mm-0.4mm, project_footprints:VIA-0.8mm-0.4mm, F.Cu at (167.4, 103.8)
- added REF**: VIA-0.8mm-0.4mm, project_footprints:VIA-0.8mm-0.4mm, F.Cu at (170.9, 103.1)
- added REF**: VIA-0.8mm-0.4mm, project_footprints:VIA-0.8mm-0.4mm, F.Cu at (170.2, 103.1)
- added REF**: VIA-0.8mm-0.4mm, project_footprints:VIA-0.8mm-0.4mm, F.Cu at (169.6, 103.1)
- added REF**: VIA-0.8mm-0.4mm, project_footprints:VIA-0.8mm-0.4mm, F.Cu at (168.8, 103.1)
- added REF**: VIA-0.8mm-0.4mm, project_footprints:VIA-0.8mm-0.4mm, F.Cu at (168.2, 103.1)
- added REF**: VIA-0.8mm-0.4mm, project_footprints:VIA-0.8mm-0.4mm, F.Cu at (167.4, 103.1)
- added REF**: VIA-0.8mm-0.4mm, project_footprints:VIA-0.8mm-0.4mm, F.Cu at (166.8, 103.1)
- added REF**: VIA-0.8mm-0.4mm, project_footprints:VIA-0.8mm-0.4mm, F.Cu at (170.9, 102.4)
- added REF**: VIA-0.8mm-0.4mm, project_footprints:VIA-0.8mm-0.4mm, F.Cu at (172.5, 92.5)
- added REF**: VIA-0.8mm-0.4mm, project_footprints:VIA-0.8mm-0.4mm, F.Cu at (170.2, 102.4)
- added REF**: VIA-0.8mm-0.4mm, project_footprints:VIA-0.8mm-0.4mm, F.Cu at (169.6, 102.4)
- added REF**: VIA-0.8mm-0.4mm, project_footprints:VIA-0.8mm-0.4mm, F.Cu at (168.8, 102.4)
- added REF**: VIA-0.8mm-0.4mm, project_footprints:VIA-0.8mm-0.4mm, F.Cu at (168.2, 102.4)
- added REF**: VIA-0.8mm-0.4mm, project_footprints:VIA-0.8mm-0.4mm, F.Cu at (167.4, 102.4)
- added REF**: VIA-0.8mm-0.4mm, project_footprints:VIA-0.8mm-0.4mm, F.Cu at (166.8, 102.4)
- added REF**: VIA-0.8mm-0.4mm, project_footprints:VIA-0.8mm-0.4mm, F.Cu at (170.9, 101.7)
- added REF**: VIA-0.8mm-0.4mm, project_footprints:VIA-0.8mm-0.4mm, F.Cu at (170.2, 101.7)
- added REF**: VIA-0.8mm-0.4mm, project_footprints:VIA-0.8mm-0.4mm, F.Cu at (169.6, 101.7)
- added REF**: VIA-0.8mm-0.4mm, project_footprints:VIA-0.8mm-0.4mm, F.Cu at (168.8, 101.7)
- added REF**: VIA-0.8mm-0.4mm, project_footprints:VIA-0.8mm-0.4mm, F.Cu at (172.5, 98.3)
- added REF**: VIA-0.8mm-0.4mm, project_footprints:VIA-0.8mm-0.4mm, F.Cu at (168.2, 101.7)
- added REF**: VIA-0.8mm-0.4mm, project_footprints:VIA-0.8mm-0.4mm, F.Cu at (167.4, 101.7)
- added REF**: VIA-0.8mm-0.4mm, project_footprints:VIA-0.8mm-0.4mm, F.Cu at (166.8, 101.7)
- added REF**: VIA-0.8mm-0.4mm, project_footprints:VIA-0.8mm-0.4mm, F.Cu at (170.9, 101.0)
- added REF**: VIA-0.8mm-0.4mm, project_footprints:VIA-0.8mm-0.4mm, F.Cu at (170.2, 101.0)
- added REF**: VIA-0.8mm-0.4mm, project_footprints:VIA-0.8mm-0.4mm, F.Cu at (169.6, 101.0)
- added REF**: VIA-0.8mm-0.4mm, project_footprints:VIA-0.8mm-0.4mm, F.Cu at (168.8, 101.0)
- added REF**: VIA-0.8mm-0.4mm, project_footprints:VIA-0.8mm-0.4mm, F.Cu at (168.2, 101.0)
- added REF**: VIA-0.8mm-0.4mm, project_footprints:VIA-0.8mm-0.4mm, F.Cu at (167.4, 101.0)
- added REF**: VIA-0.8mm-0.4mm, project_footprints:VIA-0.8mm-0.4mm, F.Cu at (166.8, 101.0)
- added REF**: VIA-0.8mm-0.4mm, project_footprints:VIA-0.8mm-0.4mm, F.Cu at (173.0, 100.5)
- added REF**: VIA-0.8mm-0.4mm, project_footprints:VIA-0.8mm-0.4mm, F.Cu at (172.4, 115.1)
- added REF**: VIA-0.8mm-0.4mm, project_footprints:VIA-0.8mm-0.4mm, F.Cu at (171.8, 115.1)
- added REF**: VIA-0.8mm-0.4mm, project_footprints:VIA-0.8mm-0.4mm, F.Cu at (171.1, 115.1)
- added REF**: VIA-0.8mm-0.4mm, project_footprints:VIA-0.8mm-0.4mm, F.Cu at (170.3, 115.1)
- added REF**: VIA-0.8mm-0.4mm, project_footprints:VIA-0.8mm-0.4mm, F.Cu at (169.7, 115.1)
- added REF**: VIA-0.8mm-0.4mm, project_footprints:VIA-0.8mm-0.4mm, F.Cu at (168.9, 115.1)
- added REF**: VIA-0.8mm-0.4mm, project_footprints:VIA-0.8mm-0.4mm, F.Cu at (168.2, 115.1)
- added REF**: VIA-0.8mm-0.4mm, project_footprints:VIA-0.8mm-0.4mm, F.Cu at (167.6, 115.1)
- added REF**: VIA-0.8mm-0.4mm, project_footprints:VIA-0.8mm-0.4mm, F.Cu at (166.8, 115.1)
- added REF**: VIA-0.8mm-0.4mm, project_footprints:VIA-0.8mm-0.4mm, F.Cu at (172.4, 114.4)
- added REF**: VIA-0.8mm-0.4mm, project_footprints:VIA-0.8mm-0.4mm, F.Cu at (172.8, 103.5)
- added REF**: VIA-0.8mm-0.4mm, project_footprints:VIA-0.8mm-0.4mm, F.Cu at (171.8, 114.4)
- added REF**: VIA-0.8mm-0.4mm, project_footprints:VIA-0.8mm-0.4mm, F.Cu at (171.1, 114.4)
- added REF**: VIA-0.8mm-0.4mm, project_footprints:VIA-0.8mm-0.4mm, F.Cu at (170.3, 114.4)
- added REF**: VIA-0.8mm-0.4mm, project_footprints:VIA-0.8mm-0.4mm, F.Cu at (169.7, 114.4)
- added REF**: VIA-0.8mm-0.4mm, project_footprints:VIA-0.8mm-0.4mm, F.Cu at (168.9, 114.4)
- added REF**: VIA-0.8mm-0.4mm, project_footprints:VIA-0.8mm-0.4mm, F.Cu at (168.2, 114.4)
- added REF**: VIA-0.8mm-0.4mm, project_footprints:VIA-0.8mm-0.4mm, F.Cu at (167.6, 114.4)
- added REF**: VIA-0.8mm-0.4mm, project_footprints:VIA-0.8mm-0.4mm, F.Cu at (166.8, 114.4)
- added REF**: VIA-0.8mm-0.4mm, project_footprints:VIA-0.8mm-0.4mm, F.Cu at (172.4, 113.7)
- added REF**: VIA-0.8mm-0.4mm, project_footprints:VIA-0.8mm-0.4mm, F.Cu at (171.8, 113.7)
- added REF**: VIA-0.8mm-0.4mm, project_footprints:VIA-0.8mm-0.4mm, F.Cu at (173.0, 107.0)
- added REF**: VIA-0.8mm-0.4mm, project_footprints:VIA-0.8mm-0.4mm, F.Cu at (171.1, 113.7)
- added REF**: VIA-0.8mm-0.4mm, project_footprints:VIA-0.8mm-0.4mm, F.Cu at (170.3, 113.7)
- added REF**: VIA-0.8mm-0.4mm, project_footprints:VIA-0.8mm-0.4mm, F.Cu at (169.7, 113.7)
- added REF**: VIA-0.8mm-0.4mm, project_footprints:VIA-0.8mm-0.4mm, F.Cu at (168.9, 113.7)
- added REF**: VIA-0.8mm-0.4mm, project_footprints:VIA-0.8mm-0.4mm, F.Cu at (168.2, 113.7)
- added REF**: VIA-0.8mm-0.4mm, project_footprints:VIA-0.8mm-0.4mm, F.Cu at (167.6, 113.7)
- added REF**: VIA-0.8mm-0.4mm, project_footprints:VIA-0.8mm-0.4mm, F.Cu at (166.8, 113.7)
- added REF**: VIA-0.8mm-0.4mm, project_footprints:VIA-0.8mm-0.4mm, F.Cu at (172.4, 113.0)
- added REF**: VIA-0.8mm-0.4mm, project_footprints:VIA-0.8mm-0.4mm, F.Cu at (171.8, 113.0)
- added REF**: VIA-0.8mm-0.4mm, project_footprints:VIA-0.8mm-0.4mm, F.Cu at (171.1, 113.0)
- added REF**: VIA-0.8mm-0.4mm, project_footprints:VIA-0.8mm-0.4mm, F.Cu at (173.0, 110.8)
- added REF**: VIA-0.8mm-0.4mm, project_footprints:VIA-0.8mm-0.4mm, F.Cu at (170.3, 113.0)
- added REF**: VIA-0.8mm-0.4mm, project_footprints:VIA-0.8mm-0.4mm, F.Cu at (169.7, 113.0)
- added REF**: VIA-0.8mm-0.4mm, project_footprints:VIA-0.8mm-0.4mm, F.Cu at (168.9, 113.0)
- added REF**: VIA-0.8mm-0.4mm, project_footprints:VIA-0.8mm-0.4mm, F.Cu at (168.2, 113.0)
- added REF**: VIA-0.8mm-0.4mm, project_footprints:VIA-0.8mm-0.4mm, F.Cu at (167.6, 113.0)
- added REF**: VIA-0.8mm-0.4mm, project_footprints:VIA-0.8mm-0.4mm, F.Cu at (166.8, 113.0)
- added REF**: VIA-0.8mm-0.4mm, project_footprints:VIA-0.8mm-0.4mm, F.Cu at (184.4, 108.8)
- added REF**: VIA-0.8mm-0.4mm, project_footprints:VIA-0.8mm-0.4mm, F.Cu at (183.8, 108.8)
- added REF**: VIA-0.8mm-0.4mm, project_footprints:VIA-0.8mm-0.4mm, F.Cu at (183.1, 108.8)
- added REF**: VIA-0.8mm-0.4mm, project_footprints:VIA-0.8mm-0.4mm, F.Cu at (136.2, 109.5)
- added REF**: VIA-0.8mm-0.4mm, project_footprints:VIA-0.8mm-0.4mm, F.Cu at (182.3, 108.8)
- added REF**: VIA-0.8mm-0.4mm, project_footprints:VIA-0.8mm-0.4mm, F.Cu at (181.7, 108.8)
- added REF**: VIA-0.8mm-0.4mm, project_footprints:VIA-0.8mm-0.4mm, F.Cu at (184.4, 108.1)
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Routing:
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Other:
- board text added: "U"
- board text added: "V"
- board text added: "W"
